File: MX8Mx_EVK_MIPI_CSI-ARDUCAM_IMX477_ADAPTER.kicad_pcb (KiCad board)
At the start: 2 copper layers, 40.5 x 40.5 mm, 13 parts, among them J1 1888863-4, J2 54548-2271, J3 54548-2271, U1 NLSX5012DMR2G, U2 PCA9306D

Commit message: Finish layout
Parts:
- removed J3: 54548-2271, footprints:MOLEX_54548-2271
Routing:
- net GND: track 156.6 -> 170.9 mm
- net /CSI_CLK_P__SPCLK_LVDS0_P: track 31.5 -> 27.8 mm, vias 1 -> 0
- net /CSI_DN1__SD_LVDS1_N: track 35.8 -> 33.2 mm
- net /CSI_DN0__SD_LVDS0_N: track 35.7 -> 33.2 mm
- net /CSI_DN3__SD_LVDS3_N: track 37.4 -> 34.8 mm
- net /CSI_DN2__SD_LVDS2_N: track 36.0 -> 33.5 mm
- net /CSI_DP1__SD_LVDS1_P: track 35.8 -> 33.7 mm
- net /CSI_DP3__SD_LVDS3_P: track 36.0 -> 34.0 mm
- net /SENS_LED_3V3: track 14.4 -> 12.4 mm, vias 1 -> 0
- net /CSI_CLK_N__SPCLK_LVDS0_N: track 30.0 -> 28.0 mm, vias 1 -> 0
- net /SENS_EN_3V3: track 14.4 -> 12.6 mm, vias 1 -> 0
- net /CSI_DP2__SD_LVDS2_P: track 36.1 -> 34.3 mm
- net /CSI_DP0__SD_LVDS0_P: track 35.1 -> 33.4 mm
- net /I2C_CLK_3V3: vias 1 -> 0
- net /I2C_DAT_3V3: vias 1 -> 0

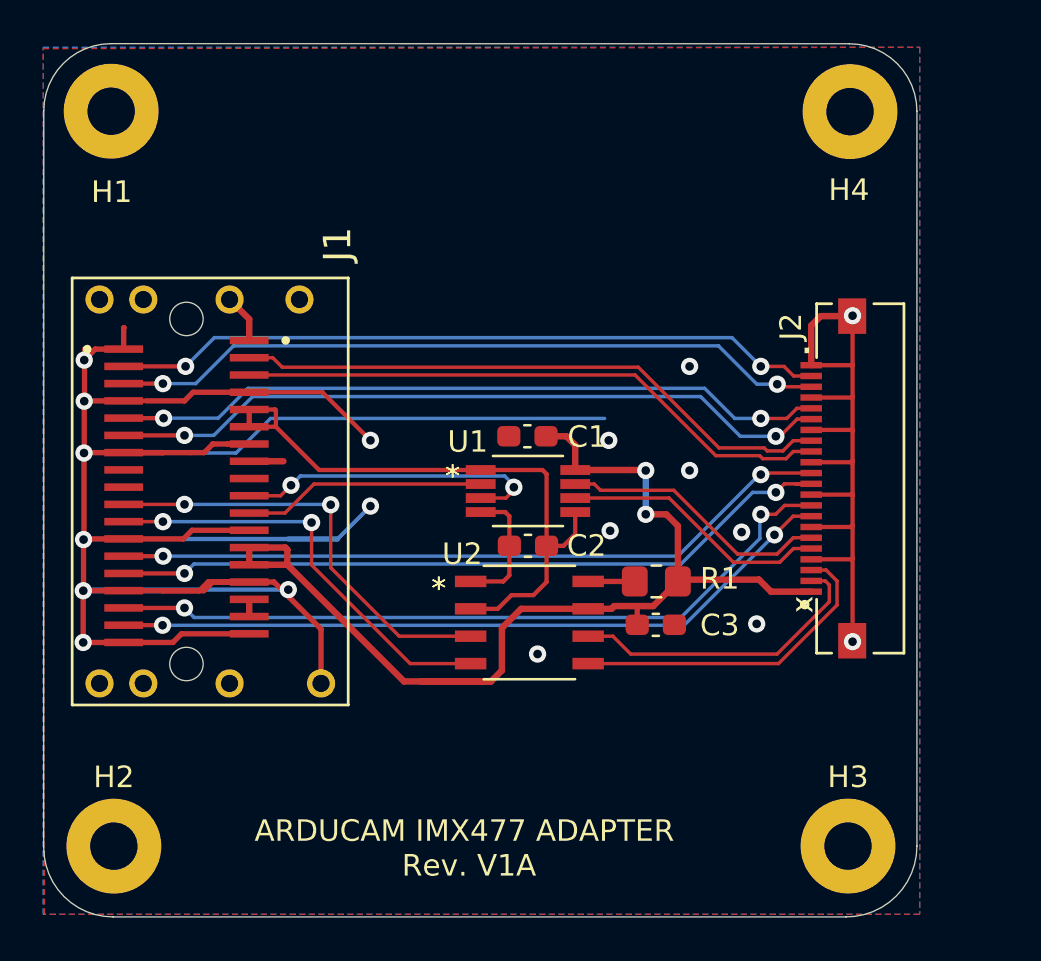
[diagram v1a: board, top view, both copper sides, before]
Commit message: Add option to select 1V8/3V3 level for signals of camera side
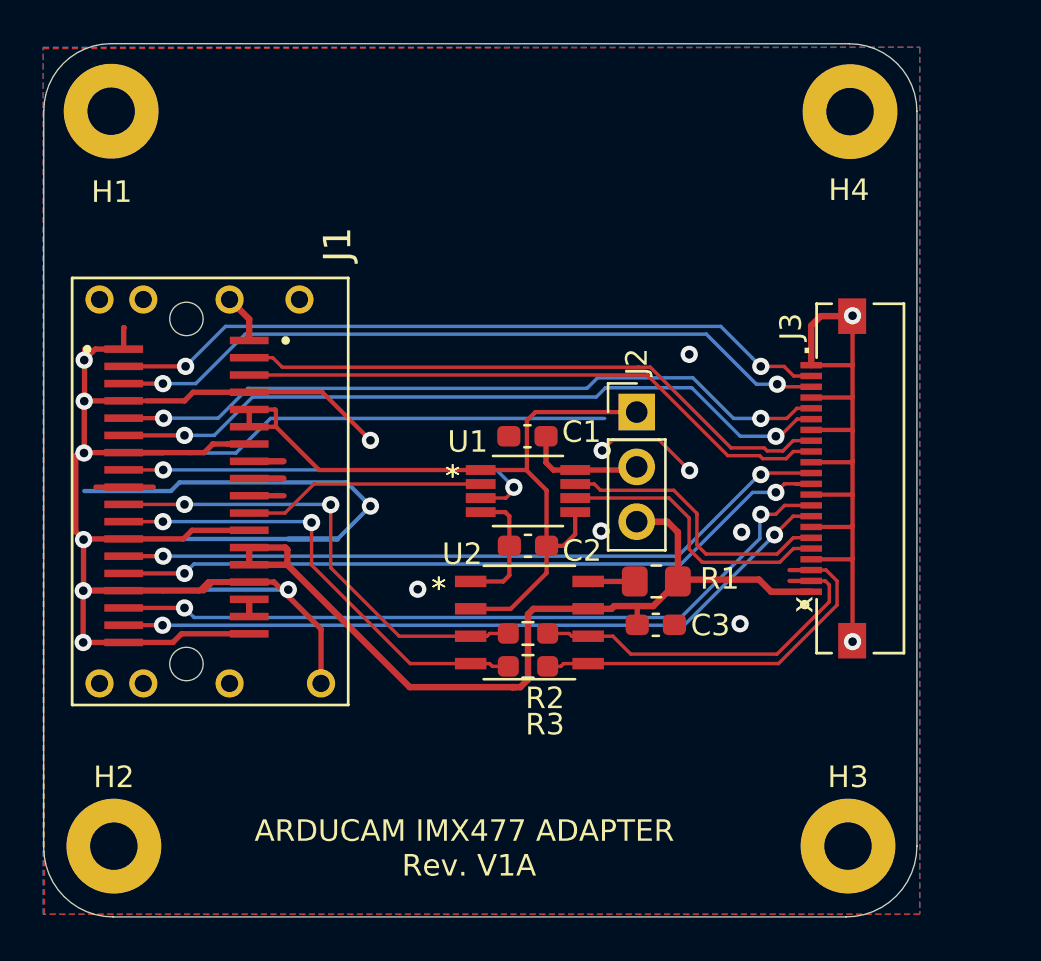
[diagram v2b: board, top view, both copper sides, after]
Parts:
- added J2: Conn_01x03_Male, Connector_PinHeader_2.54mm:PinHeader_1x03_P2.54mm_Vertical, F.Cu at (129.8, 93.1)
- added R2: 0, Resistor_SMD:R_0603_1608Metric_Pad0.98x0.95mm_HandSolder, F.Cu at (124.7, 103.4)
- added R3: 0, Resistor_SMD:R_0603_1608Metric_Pad0.98x0.95mm_HandSolder, F.Cu at (124.7, 104.9)
- renumbered J2 to J3
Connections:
- C1 pad 1: +3V3 -> VCC
- U1 pad 3: /CSI_SYNC_1V8 -> /CSI_MCLK_1V8
- U1 pad 8: +3V3 -> VCC
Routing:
- net /CSI_MCLK_1V8: track 0.00 -> 20.5 mm, vias 0 -> 2
- net GND: track 170.9 -> 190.1 mm
- net /CSI_SYNC_1V8: track 14.9 -> 1.61 mm, vias 2 -> 0
- net +3V3: track 51.3 -> 41.2 mm, vias 2 -> 0
- net +1V8: track 29.1 -> 36.0 mm
- net VCC: track 0.00 -> 5.66 mm
- net /I2C_DAT_3V3: track 14.2 -> 17.2 mm
- net /I2C_CLK_3V3: track 15.2 -> 18.1 mm
- net /CSI_nRST_1V8: track 0.00 -> 2.66 mm
- net /I2C_SCL_1V8: track 20.0 -> 21.8 mm
- net /I2C_SDA_1V8: track 20.3 -> 22.1 mm
- net Net-(J1-PadB9): track 0.00 -> 1.58 mm
- net /SENS_EN_3V3: track 12.6 -> 13.5 mm
- net /SENS_LED_3V3: track 12.4 -> 13.3 mm

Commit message: Optimize routing
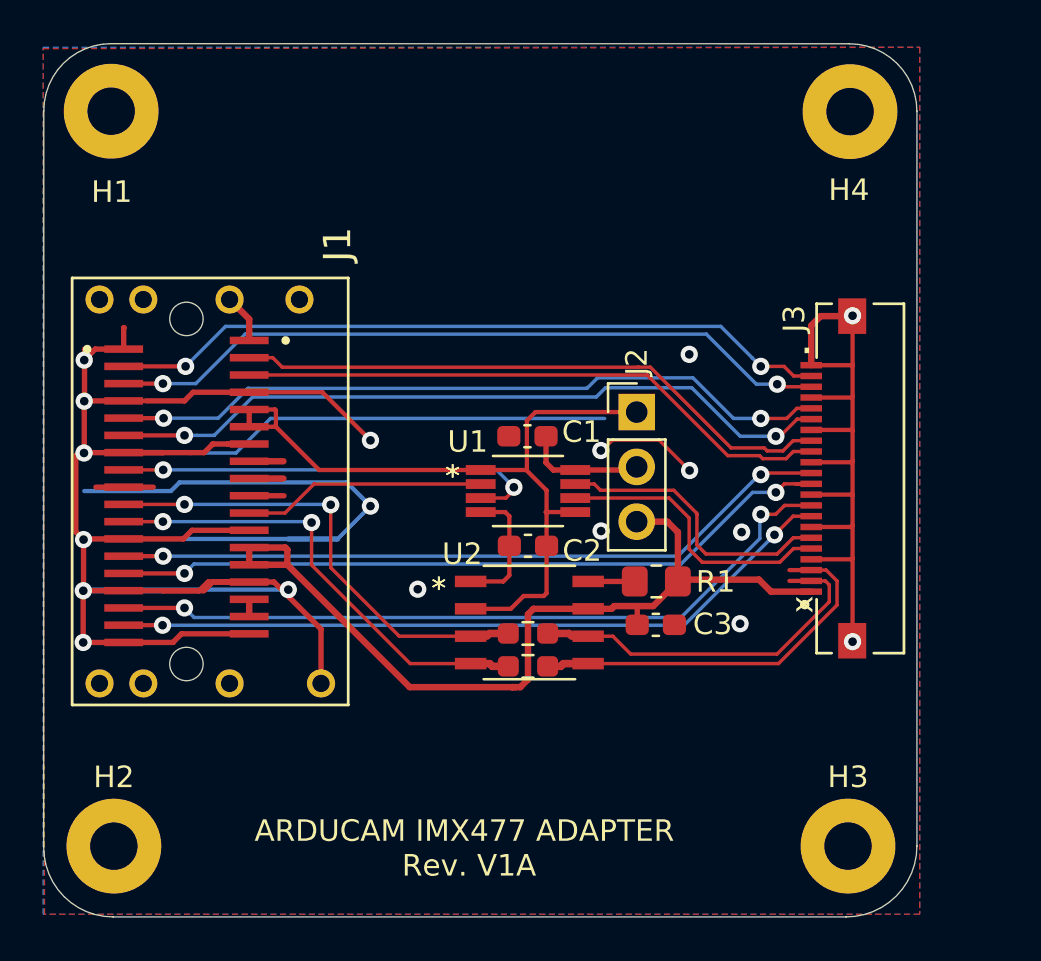
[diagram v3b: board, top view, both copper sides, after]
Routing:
- net +1V8: track 36.0 -> 35.4 mm
